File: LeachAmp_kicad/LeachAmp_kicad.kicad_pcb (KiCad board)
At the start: 2 copper layers, 262.4 x 104.9 mm, 124 parts, among them J1 , J2 , J3 Conn_01x03_Female, J4 Conn_01x03_Female, Q1 BC546, Q10 MPSA06, Q11 MPSA56, Q12 BF470, Q13 BF469, Q14 BF469, Q15 BF470, Q16 MJE15030, Q17 MJE15031, Q2 BC546, Q3 BC556, Q4 BC556, Q5 BC546, Q6 BC556, Q8 BC556, Q9 BC546, T1 MJL3281, T2 MJL3201, T3 MJL3281, T4 MJL3201

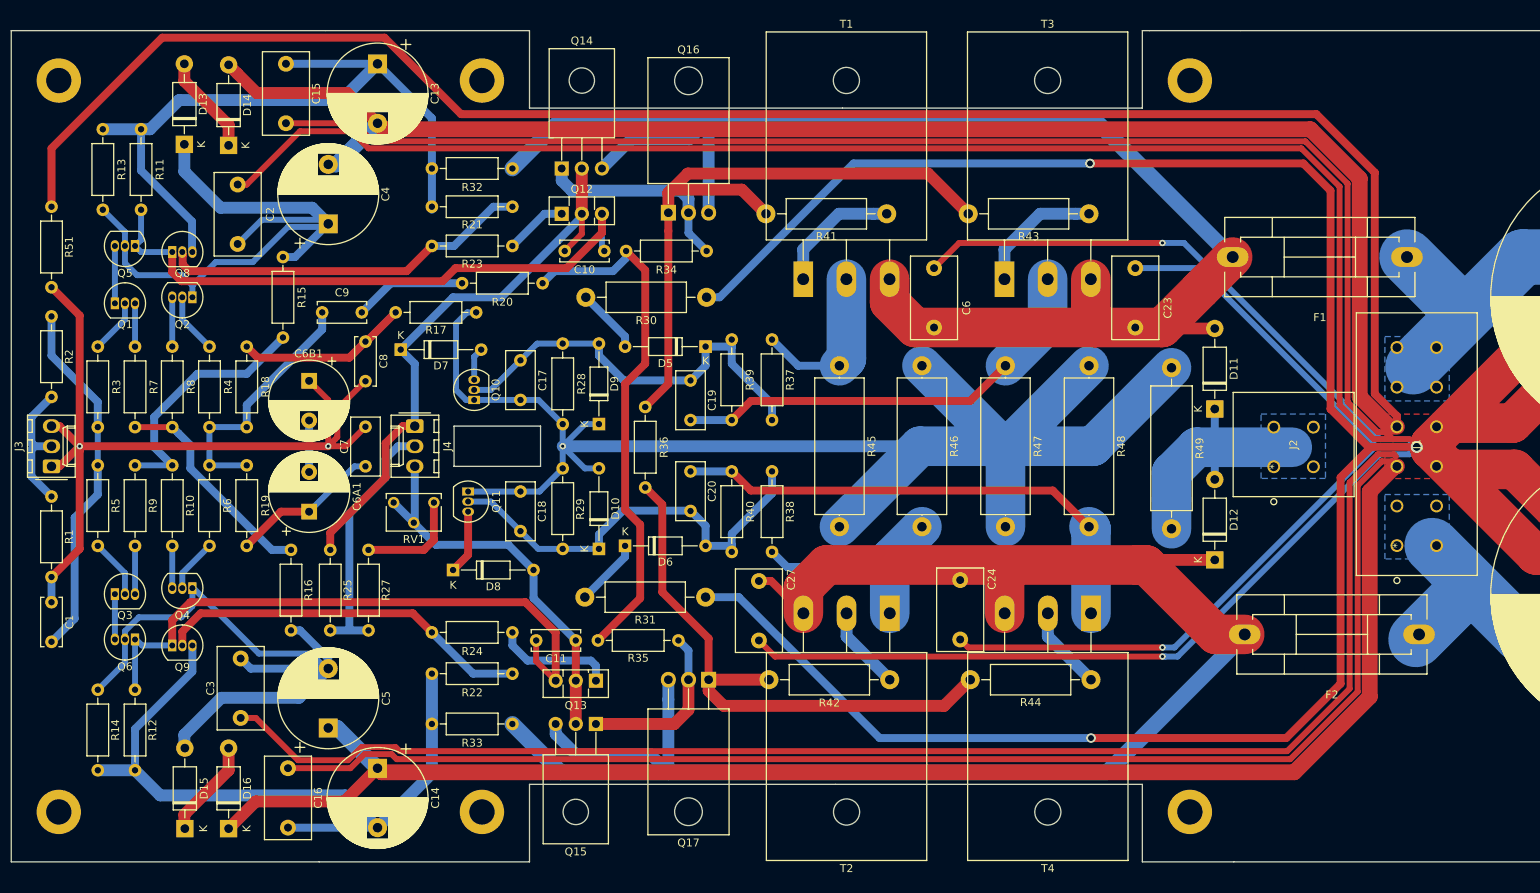
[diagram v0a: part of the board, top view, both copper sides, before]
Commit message: nove_rozmery_soucastek
Nové rozměry součástek hlavně u kondenzátorů
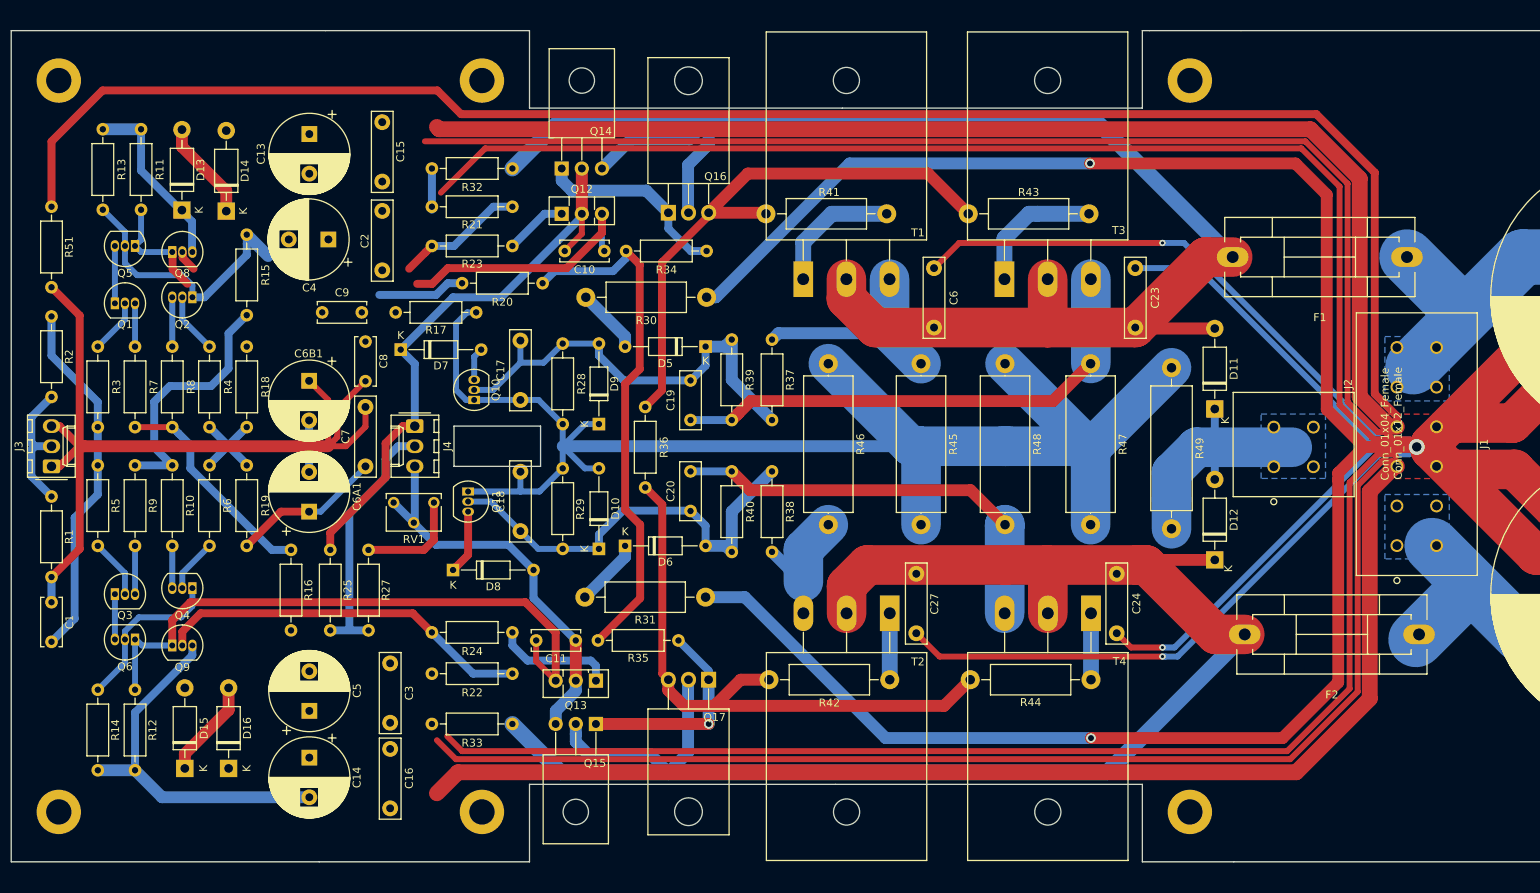
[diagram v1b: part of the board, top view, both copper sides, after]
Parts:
- C13, C14, C4, C5: footprint Capacitor_THT:CP_Radial_D12.5mm_P7.50mm -> Capacitor_THT:CP_Radial_D10.0mm_P5.00mm
- C15, C16, C2, C23, C24, C27, C3, C6: footprint Capacitor_THT:C_Rect_L10.3mm_W5.7mm_P7.50mm_MKS4 -> Capacitor_THT:C_Rect_L10.0mm_W2.5mm_P7.50mm_MKS4
- C17, C18, C7: footprint Capacitor_THT:C_Rect_L7.2mm_W3.5mm_P5.00mm_FKS2_FKP2_MKS2_MKP2 -> Capacitor_THT:C_Rect_L10.0mm_W2.5mm_P7.50mm_MKS4
- C19, C20: footprint Capacitor_THT:C_Rect_L7.2mm_W3.5mm_P5.00mm_FKS2_FKP2_MKS2_MKP2 -> Capacitor_THT:C_Rect_L7.2mm_W2.5mm_P5.00mm_FKS2_FKP2_MKS2_MKP2
- J1: value (none) -> Conn_01x12_Female
- J2: value (none) -> Conn_01x04_Female
- moved C27 19.9 mm to (185.8, 115.0)
- moved C24 19.8 mm to (211.1, 107.5)
- moved C3 18.9 mm to (119.4, 126.3)
- moved C2 18.5 mm to (118.4, 61.7)
- moved C15 14.2 mm to (118.4, 50.5)
- moved C16 13.1 mm to (119.4, 129.6)
- moved C13 12.4 mm to (109.2, 52.0)
- moved R46 11.8 mm to (174.7, 101.3)
- moved R47 10.7 mm to (207.8, 101.3)
- moved R48 10.6 mm to (197.0, 101.3)
- moved R45 10.3 mm to (186.4, 101.3)
- moved C14 8.71 mm to (109.2, 130.7)
- moved D14 8.31 mm to (98.7, 61.8)
- moved D13 8.31 mm to (93.1, 61.6)
- moved D15 7.60 mm to (93.5, 132.1)
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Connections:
- Q15 pad 2: Net-(C11-Pad1) -> Net-(C24-Pad1)
- Q15 pad 3: Net-(C24-Pad1) -> Net-(C11-Pad1)
- Q16 pad 1: Net-(Q16-Pad1) -> Net-(Q14-Pad1)
- Q16 pad 2: Net-(Q14-Pad1) -> Net-(C23-Pad2)
- Q16 pad 3: Net-(C23-Pad2) -> Net-(Q16-Pad3)
- Q17 pad 1: Net-(Q17-Pad1) -> Net-(Q15-Pad1)
- Q17 pad 2: Net-(Q15-Pad1) -> Net-(C24-Pad1)
- Q17 pad 3: Net-(C24-Pad1) -> Net-(Q17-Pad3)
- R36 pad 1: Net-(Q16-Pad1) -> Net-(Q16-Pad3)
- R36 pad 2: Net-(Q17-Pad1) -> Net-(Q17-Pad3)
- R41 pad 1: Net-(Q16-Pad1) -> Net-(Q16-Pad3)
- R42 pad 1: Net-(Q17-Pad1) -> Net-(Q17-Pad3)
- R43 pad 1: Net-(Q16-Pad1) -> Net-(Q16-Pad3)
- R44 pad 1: Net-(Q17-Pad1) -> Net-(Q17-Pad3)
- T1 pad 2: Net-(R37-Pad1) -> Net-(C23-Pad2)
- T1 pad 3: Net-(C23-Pad2) -> Net-(R37-Pad1)
- T2 pad 1: Net-(R38-Pad1) -> Net-(R42-Pad2)
- T2 pad 2: Net-(R42-Pad2) -> Net-(C24-Pad1)
- T2 pad 3: Net-(C24-Pad1) -> Net-(R38-Pad1)
- T3 pad 2: Net-(C19-Pad1) -> Net-(C23-Pad2)
- T3 pad 3: Net-(C23-Pad2) -> Net-(C19-Pad1)
- T4 pad 1: Net-(C20-Pad2) -> Net-(R44-Pad2)
- T4 pad 2: Net-(R44-Pad2) -> Net-(C24-Pad1)
- T4 pad 3: Net-(C24-Pad1) -> Net-(C20-Pad2)
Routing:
- net GND: track 2025.4 -> 1819.3 mm
- net Net-(Q16-Pad1): track 82.9 -> 0.00 mm
- net Net-(Q17-Pad3): track 0.00 -> 75.3 mm
- net Net-(Q16-Pad3): track 0.00 -> 72.0 mm
- net Net-(Q17-Pad1): track 71.8 -> 0.00 mm
- net Net-(C3-Pad2): track 84.5 -> 21.0 mm
- net Net-(C13-Pad1): track 89.1 -> 28.2 mm
- net Net-(C2-Pad2): track 84.1 -> 34.5 mm
- net Net-(C14-Pad2): track 90.6 -> 46.9 mm
- net Net-(C10-Pad2): track 77.0 -> 48.0 mm
- net Net-(Q8-Pad2): track 46.9 -> 19.0 mm
- net Net-(C8-Pad1): track 21.7 -> 0.13 mm
- net Net-(C9-Pad1): track 32.6 -> 13.5 mm
- net Net-(C24-Pad1): track 217.1 -> 205.1 mm
- net Net-(C20-Pad2): track 64.2 -> 53.7 mm
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
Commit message: oprava DPS
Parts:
- moved C4 2.53 mm to (109.2, 66.1), turned to 90 degrees
- moved C13 2.30 mm to (109.2, 49.7)
- moved C15 2.10 mm to (118.4, 48.4)
- moved C2 1.80 mm to (118.4, 59.9)
- moved R11 0.80 mm to (87.2, 51.4)
- moved R13 0.80 mm to (82.3, 51.4)
- moved C14 0.50 mm to (109.2, 131.2)
- moved C16 0.40 mm to (119.4, 130.0)
- moved C3 0.40 mm to (119.4, 125.9)
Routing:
- net GND: track 1819.3 -> 1917.4 mm
- net Net-(C3-Pad2): track 21.0 -> 71.5 mm
- net Net-(C13-Pad1): track 28.2 -> 53.7 mm
- net Net-(C14-Pad2): track 46.9 -> 57.6 mm
- net Net-(C2-Pad2): track 34.5 -> 40.8 mm
